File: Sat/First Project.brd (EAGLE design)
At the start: 100 x 80 mm, 22 parts, among them U1 ATMEGA328P_TQFP, U2 915MHz, U3 9DoF IMU, U4 3.3V/150mA

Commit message: Finished Schematic
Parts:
- removed R5, R6, R7: 10K, femtosat:0603-RES
- removed SJ1: (no value), jumper:SJ_2
- moved J2 87.0 mm to (103.3, 2.88)
- moved U3 81.0 mm to (110.8, 63.3), flipped to the bottom, turned to 177.3 degrees
- moved U1 72.8 mm to (113.6, 54.4)
- moved C1 69.4 mm to (107.2, 56.8)
- moved C2 68.7 mm to (102.9, 65.0)
- moved U4 65.8 mm to (110.0, 36.9)
- moved ANT1 63.8 mm to (106.9, 24.6)
- moved TP1 63.0 mm to (101.6, 22.8)
- moved J1 62.6 mm to (121.0, 59.1), turned to 90 degrees
- moved B1 59.9 mm to (115.6, 12.5)
- moved U2 58.0 mm to (114.5, 36.0), turned to 270 degrees
- moved R1 53.1 mm to (106.4, 64.2)
- moved D1 50.0 mm to (102.0, 37.5), turned to 270 degrees
- moved TP2 48.8 mm to (101.3, 57.0)
- moved R4 45.4 mm to (102.5, 60.9)
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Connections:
- removed net AD0/ASO: SJ1.1
- removed net AUX_CL: U3.7
- removed net AUX_DA: U3.21
- removed net CS: R7.1, U3.22
- removed net INT: U3.12
- removed net N$10: C3.1, U3.10
- removed net N$12: SJ1.2, U3.9
- removed net VDDIO: U3.1, U3.8
- net 12C_SCL: no longer R5.1
- net 12C_SDA: no longer R6.1
- net 3.3V: now also U3.1, U3.8; no longer R5.2, R6.2, R7.2
- net FSYNC: now also C3.1, U3.10; no longer U3.11
- net GND: now also U3.11, U3.21, U3.7, U3.9; no longer SJ1.3
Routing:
- net N$2: track 0.00 -> 900.9 mm
- net GND: track 0.00 -> 119.1 mm
- net 3.3V: track 0.00 -> 67.7 mm, vias 0 -> 4
- net 12C_SDA: track 0.00 -> 63.1 mm, vias 0 -> 3
- net 12C_SCL: track 0.00 -> 49.8 mm
- net DIO_0: track 0.00 -> 44.5 mm, vias 0 -> 2
- net VBAT: track 0.00 -> 37.4 mm
- net FSYNC: track 0.00 -> 29.8 mm, vias 0 -> 3
- net N$9: track 0.00 -> 20.6 mm
- net DTR: track 0.00 -> 19.8 mm
- net N$1: track 0.00 -> 16.7 mm
- net SPI_SCK: track 0.00 -> 16.7 mm
- net TXO: track 0.00 -> 11.4 mm
- net RXI: track 0.00 -> 9.54 mm
- net SPI_MISO: track 0.00 -> 7.86 mm
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- removed copper zone on layer 1, net POLLYWOLLY
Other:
- board size 100 x 80 mm -> 25 x 70 mm

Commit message: Routed Components and added a Ground Plane
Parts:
- removed J2: (no value), femtosat:1X02
- added C4: 0.1uF, femtosat:0603-CAP
- added C5: 1.0uF, femtosat:0603
- added J3: (no value), femtosat:JST-2-SMD
- moved TP1 39.6 mm to (114.1, 60.3)
- moved ANT1 20.5 mm to (105.0, 45.0)
- moved U4 19.8 mm to (102.6, 18.5)
- moved R3 18.8 mm to (120.8, 63.0), turned to 180 degrees
- moved R4 18.6 mm to (120.8, 64.5), turned to 180 degrees
- moved C2 18.2 mm to (120.8, 68.0), turned to 180 degrees
- moved R1 14.5 mm to (120.8, 66.0), turned to 180 degrees
- moved D1 12.6 mm to (103.7, 50.0), turned to 0 degrees
- moved R2 10.3 mm to (103.7, 51.7)
- moved C3 9.74 mm to (102.6, 58.3)
- moved TP2 8.42 mm to (108.8, 60.8)
- moved U3 6.24 mm to (104.8, 65.0), flipped to the top, turned to 180 degrees
- moved J1 5.52 mm to (123.0, 54.0)
- moved C1 4.84 mm to (102.6, 55.4)
- moved B1 3.62 mm to (112.0, 13.0)
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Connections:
- removed net VBAT: J2.2, U4.1
- new net N$2: J3.2, U4.1
- net 3.3V: now also C4.1, C5.1
- net GND: now also C4.2, C5.2, J3.1; no longer J2.1
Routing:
- net N$2: track 900.9 -> 15.3 mm
- net GND: track 119.1 -> 22.2 mm, vias 0 -> 4
- net 3.3V: track 67.7 -> 133.9 mm, vias 4 -> 3
- net 12C_SDA: track 63.1 -> 25.0 mm, vias 3 -> 2
- net VBAT: track 37.4 -> 0.00 mm
- net 12C_SCL: track 49.8 -> 30.2 mm, vias 0 -> 2
- net SPI_MISO: track 7.86 -> 26.2 mm
- net FSYNC: track 29.8 -> 11.9 mm, vias 3 -> 0
- net SPI_MOSI: track 7.39 -> 24.2 mm
- net DIO_0: track 44.5 -> 29.7 mm, vias 2 -> 0
- net N$9: track 20.6 -> 6.44 mm
- net SPI_SS: track 7.13 -> 19.3 mm
- net DTR: track 19.8 -> 10.0 mm
- net N$1: track 16.7 -> 22.0 mm, vias 0 -> 2
- net RXI: track 9.54 -> 14.2 mm, vias 0 -> 2
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- added copper zone on layer 1, net GND
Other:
- board size 25 x 70 mm -> 25 x 69.8 mm

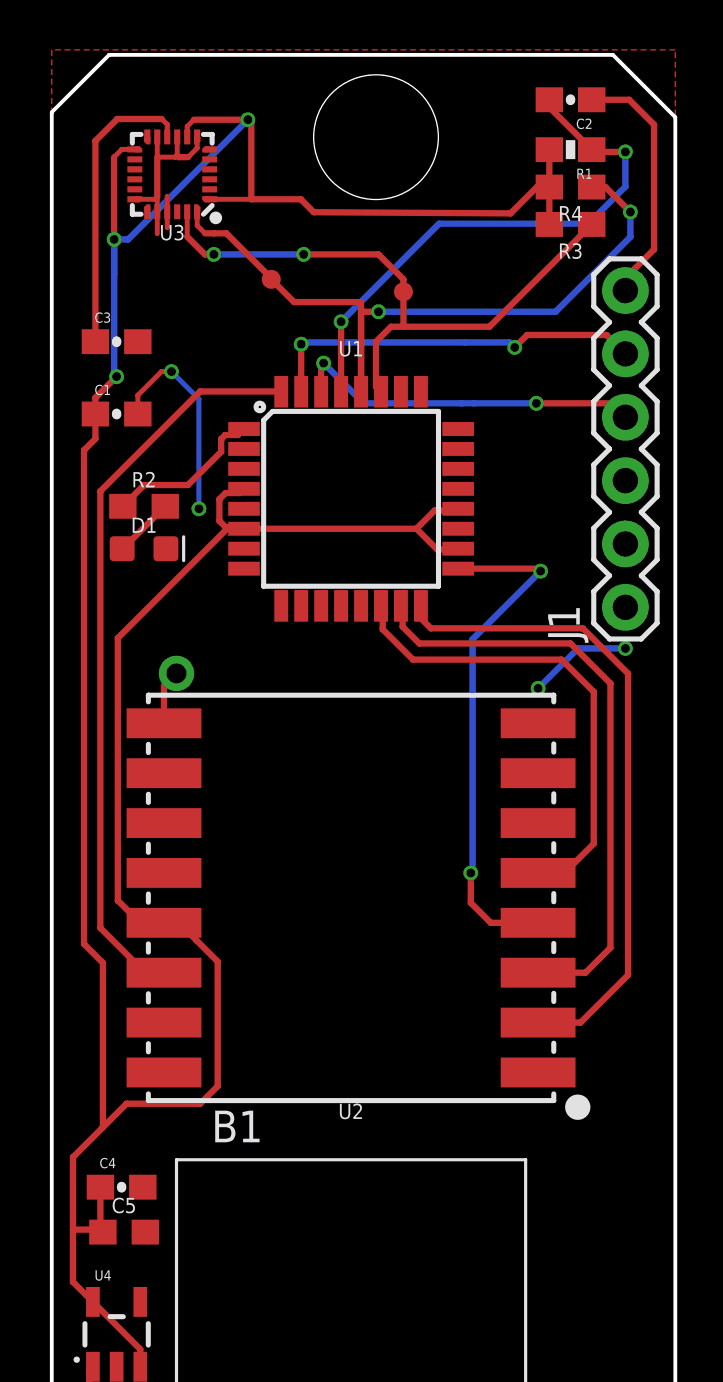
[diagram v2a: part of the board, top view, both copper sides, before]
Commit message: Cleaned up some routing
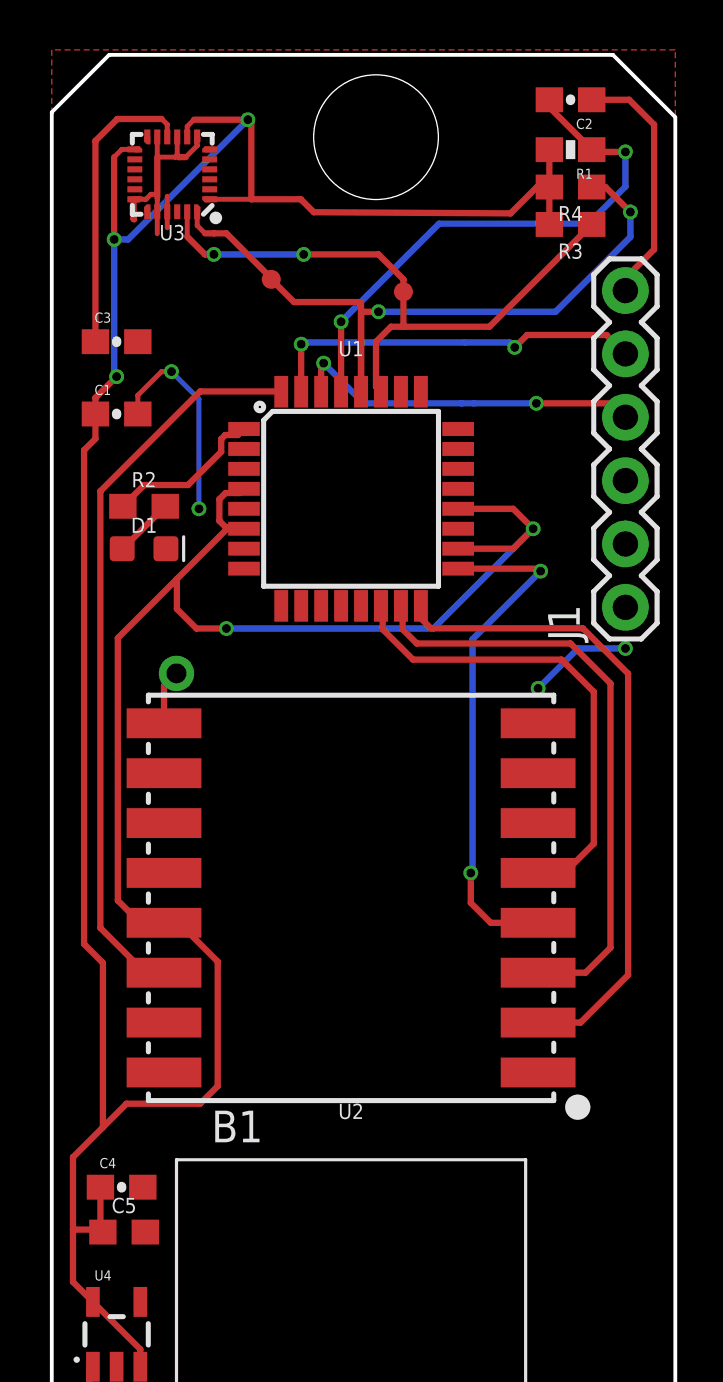
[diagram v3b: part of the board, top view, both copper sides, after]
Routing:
- net 3.3V: track 133.9 -> 145.9 mm, vias 3 -> 5
- net GND: track 22.2 -> 23.1 mm
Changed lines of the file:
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@@
 <vertex x="100" y="70"/>
 </polygon>
-<wire x1="104.23" y1="63.51" x2="104.23" y2="62.63" width="0.2" layer="1"/>
+<wire x1="104.23" y1="62.63" x2="104.23" y2="63.51" width="0.2" layer="1"/>
 <wire x1="104.63" y1="63.51" x2="104.63" y2="62.87" width="0.2" layer="1"/>
-<wire x1="104.23" y1="63.51" x2="104.23" y2="64.1" width="0.2" layer="1"/>
+<wire x1="104.23" y1="64" x2="104.23" y2="64.21" width="0.2" layer="1"/>
 <wire x1="104.23" y1="64.1" x2="104.23" y2="65.7" width="0.254" layer="1"/>
 <wire x1="104.23" y1="65.7" x2="104.23" y2="66.51" width="0.2" layer="1"/>
 <wire x1="105.03" y1="66.51" x2="105.03" y2="65.77" width="0.2" layer="1"/>
 <wire x1="105.03" y1="65.77" x2="105.1" y2="65.7" width="0.254" layer="1"/>
-<wire x1="105.1" y1="65.7" x2="105.470675" y2="65.7" width="0.254" layer="1"/>
-<wire x1="105.470675" y1="65.7" x2="105.83" y2="66.059325" width="0.2" layer="1"/>
-<wire x1="105.83" y1="66.059325" x2="105.83" y2="66.5625" width="0.2" layer="1"/>
+<wire x1="105.1" y1="65.7" x2="105.370675" y2="65.7" width="0.254" layer="1"/>
+<wire x1="105.370675" y1="65.7" x2="105.83" y2="66.159325" width="0.2" layer="1"/>
+<wire x1="105.83" y1="66.159325" x2="105.83" y2="66.5625" width="0.2" layer="1"/>
 <wire x1="104.23" y1="65.7" x2="104.96" y2="65.7" width="0.2" layer="1"/>
 <wire x1="104.96" y1="65.7" x2="105.03" y2="65.77" width="0.2" layer="1"/>
@@
 <wire x1="105.9" y1="56" x2="105.9" y2="51.6" width="0.2" layer="16"/>
 <via x="105.9" y="51.6" extent="1-16" drill="0.35"/>
-<wire x1="103.2775" y1="64.01" x2="104.14" y2="64.01" width="0.2" layer="1"/>
-<wire x1="104.14" y1="64.01" x2="104.23" y2="64.1" width="0.2" layer="1"/>
+<wire x1="103.9775" y1="64.21" x2="104.23" y2="64.21" width="0.2" layer="1"/>
 <wire x1="104.63" y1="63.51" x2="104.63" y2="64.13" width="0.2" layer="1"/>
+<wire x1="103.2775" y1="64.01" x2="103.2775" y2="63.2225" width="0.254" layer="1"/>
+<wire x1="103.2775" y1="63.2225" x2="103.3" y2="63.2" width="0.254" layer="1"/>
+<wire x1="104.23" y1="63.51" x2="104.23" y2="64" width="0.2" layer="1"/>
+<wire x1="103.7775" y1="64.01" x2="103.9775" y2="64.21" width="0.2" layer="1"/>
+<wire x1="103.2775" y1="64.01" x2="103.7775" y2="64.01" width="0.2" layer="1"/>
 </signal>
 <signal name="TXO">
@@
 <wire x1="119.95" y1="64.5" x2="119.95" y2="63" width="0.254" layer="1"/>
 <via x="102.5" y="62.4" extent="1-16" drill="0.35"/>
-<wire x1="102.5" y1="62.4" x2="102.5" y2="61" width="0.254" layer="16"/>
 <via x="102.6" y="56.9" extent="1-16" drill="0.35"/>
-<wire x1="102.5" y1="61" x2="102.5" y2="57" width="0.254" layer="16"/>
+<wire x1="102.5" y1="62.4" x2="102.5" y2="57" width="0.254" layer="16"/>
 <wire x1="102.6" y1="56.9" x2="101.75" y2="56.05" width="0.254" layer="1"/>
 <wire x1="101.75" y1="56.05" x2="101.75" y2="55.4" width="0.254" layer="1"/>
@@
 <wire x1="106.96785" y1="50.8682" x2="107.6392" y2="50.8682" width="0.254" layer="1"/>
 <wire x1="107.6392" y1="50.8682" x2="107.7074" y2="50.8" width="0.254" layer="1"/>
-<wire x1="115.35305" y1="51.5318" x2="116.2244" y2="51.5318" width="0.254" layer="1"/>
 <wire x1="116.2244" y1="51.5318" x2="116.2926" y2="51.6" width="0.254" layer="1"/>
 <wire x1="107.7074" y1="50.8" x2="107.8" y2="50.8" width="0.3" layer="1"/>
-<wire x1="114.62125" y1="50.8" x2="115.35305" y2="51.5318" width="0.254" layer="1"/>
-<wire x1="115.45305" y1="49.9682" x2="116.2608" y2="49.9682" width="0.254" layer="1"/>
-<wire x1="114.62125" y1="50.8" x2="115.45305" y2="49.9682" width="0.254" layer="1"/>
 <wire x1="101.65" y1="19.8001" x2="103.55" y2="17.9001" width="0.254" layer="1"/>
 <wire x1="103.55" y1="17.9001" x2="103.55" y2="17.1999" width="0.254" layer="1"/>
@@
 <wire x1="106.6524" y1="28.4524" x2="105.9476" y2="27.7476" width="0.254" layer="1"/>
 <wire x1="105.9476" y1="27.7476" x2="102.9976" y2="27.7476" width="0.254" layer="1"/>
-<wire x1="106.6524" y1="33.4476" x2="105.8" y2="34.3" width="0.254" layer="1"/>
+<wire x1="106.6524" y1="33.4476" x2="105.1" y2="35" width="0.254" layer="1"/>
 <wire x1="104.5" y1="35" x2="105.1" y2="35" width="0.254" layer="1"/>
-<wire x1="105.1" y1="35" x2="105.8" y2="34.3" width="0.254" layer="1"/>
 <wire x1="103.19545" y1="35.3476" x2="102.6476" y2="35.89545" width="0.254" layer="1"/>
 <wire x1="107.03145" y1="50.8" x2="107.8" y2="50.8" width="0.254" layer="1"/>
@@
 <wire x1="104.1524" y1="35.3476" x2="103.19545" y2="35.3476" width="0.254" layer="1"/>
 <wire x1="102.6476" y1="35.89545" x2="102.6476" y2="46.41615" width="0.254" layer="1"/>
-<wire x1="102.6476" y1="46.41615" x2="107.03145" y2="50.8" width="0.254" layer="1"/>
+<wire x1="102.6476" y1="46.41615" x2="105.015725" y2="48.784275" width="0.254" layer="1"/>
+<wire x1="105.015725" y1="48.784275" x2="107.03145" y2="50.8" width="0.254" layer="1"/>
 <wire x1="101.2952" y1="53.950525" x2="101.2952" y2="34.149475" width="0.254" layer="1"/>
 <wire x1="101.75" y1="55.4" x2="101.75" y2="54.405325" width="0.254" layer="1"/>
@@
 <wire x1="102.05" y1="26.8" x2="102.05" y2="33.394675" width="0.254" layer="1"/>
 <wire x1="102.9976" y1="27.7476" x2="102.05" y2="26.8" width="0.254" layer="1"/>
-<wire x1="107.8" y1="50.8" x2="114.62125" y2="50.8" width="0.254" layer="1"/>
 <wire x1="116.2608" y1="49.9682" x2="116.2926" y2="50" width="0.254" layer="1"/>
 <contactref element="C4" pad="1"/>
@@
 <wire x1="101.95" y1="24.4" x2="101.95" y2="22.7" width="0.254" layer="1"/>
 <wire x1="101.95" y1="22.7" x2="102.05" y2="22.6" width="0.1524" layer="1"/>
-<wire x1="101.65" y1="22.7" x2="100.85" y2="22.7" width="0.254" layer="1"/>
+<wire x1="101.95" y1="22.7" x2="100.85" y2="22.7" width="0.254" layer="1"/>
 <wire x1="101.65" y1="19.8001" x2="100.85" y2="20.6001" width="0.254" layer="1"/>
-<wire x1="101.95" y1="22.7" x2="101.65" y2="22.7" width="0.254" layer="1"/>
 <wire x1="102.6" y1="56.9" x2="102.5" y2="57" width="0.254" layer="16"/>
 <wire x1="119.45" y1="64.5" x2="118.394365625" y2="63.444365625" width="0.254" layer="1"/>
 <wire x1="119.95" y1="64.5" x2="119.45" y2="64.5" width="0.254" layer="1"/>
 <wire x1="119.95" y1="66" x2="119.95" y2="64.5" width="0.254" layer="1"/>
-<wire x1="102.5" y1="61" x2="102.5" y2="62.4" width="0.254" layer="16"/>
 <wire x1="106.3825" y1="64.01" x2="108" y2="64.01" width="0.2" layer="1"/>
 <wire x1="108" y1="64.01" x2="109.98589375" y2="64.01" width="0.254" layer="1"/>
@@
 <wire x1="107.8606" y1="67.2" x2="108" y2="67.0606" width="0.254" layer="1"/>
 <wire x1="108" y1="67.0606" x2="108" y2="64.01" width="0.254" layer="1"/>
+<wire x1="105.015725" y1="48.784275" x2="105.015725" y2="47.584275" width="0.254" layer="1"/>
+<wire x1="105.015725" y1="47.584275" x2="105.8" y2="46.8" width="0.254" layer="1"/>
+<wire x1="105.8" y1="46.8" x2="107" y2="46.8" width="0.254" layer="1"/>
+<via x="107" y="46.8" extent="1-16" drill="0.35"/>
+<wire x1="107" y1="46.8" x2="115.3" y2="46.8" width="0.254" layer="16"/>
+<wire x1="115.3" y1="46.8" x2="119.3" y2="50.8" width="0.254" layer="16"/>
+<via x="119.3" y="50.8" extent="1-16" drill="0.35"/>
+<wire x1="119.3" y1="50.8" x2="118.5" y2="50" width="0.254" layer="1"/>
+<wire x1="118.5" y1="50" x2="116.2926" y2="50" width="0.254" layer="1"/>
+<wire x1="119.3" y1="50.8" x2="118.5" y2="51.6" width="0.254" layer="1"/>
+<wire x1="118.5" y1="51.6" x2="116.2926" y2="51.6" width="0.254" layer="1"/>
 </signal>
 <signal name="SPI_SCK">
@@
 <contactref element="U2" pad="3"/>
 <wire x1="114" y1="47.7074" x2="114.0682" y2="47.6392" width="0.254" layer="1"/>
-<wire x1="114.0682" y1="47.6392" x2="114.0682" y2="46.86785" width="0.254" layer="1"/>
-<wire x1="114.0682" y1="46.86785" x2="114.73605" y2="46.2" width="0.254" layer="1"/>
-<wire x1="114.73605" y1="46.2" x2="120.8" y2="46.2" width="0.254" layer="1"/>
+<wire x1="114.0682" y1="47.6392" x2="114.0682" y2="46.76785" width="0.254" layer="1"/>
+<wire x1="114.0682" y1="46.76785" x2="114.63605" y2="46.2" width="0.254" layer="1"/>
+<wire x1="114.63605" y1="46.2" x2="120.8" y2="46.2" width="0.254" layer="1"/>
 <wire x1="120.8" y1="46.2" x2="122.4" y2="44.6" width="0.254" layer="1"/>
 <wire x1="122.4" y1="44.6" x2="122.4" y2="34" width="0.254" layer="1"/>
